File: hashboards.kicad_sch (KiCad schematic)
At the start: 5 parts, among them J10 Hashboard3, J4 Hashboard0, J5 Hashboard1, J9 Hashboard2, U10 PCA9546ARGVR

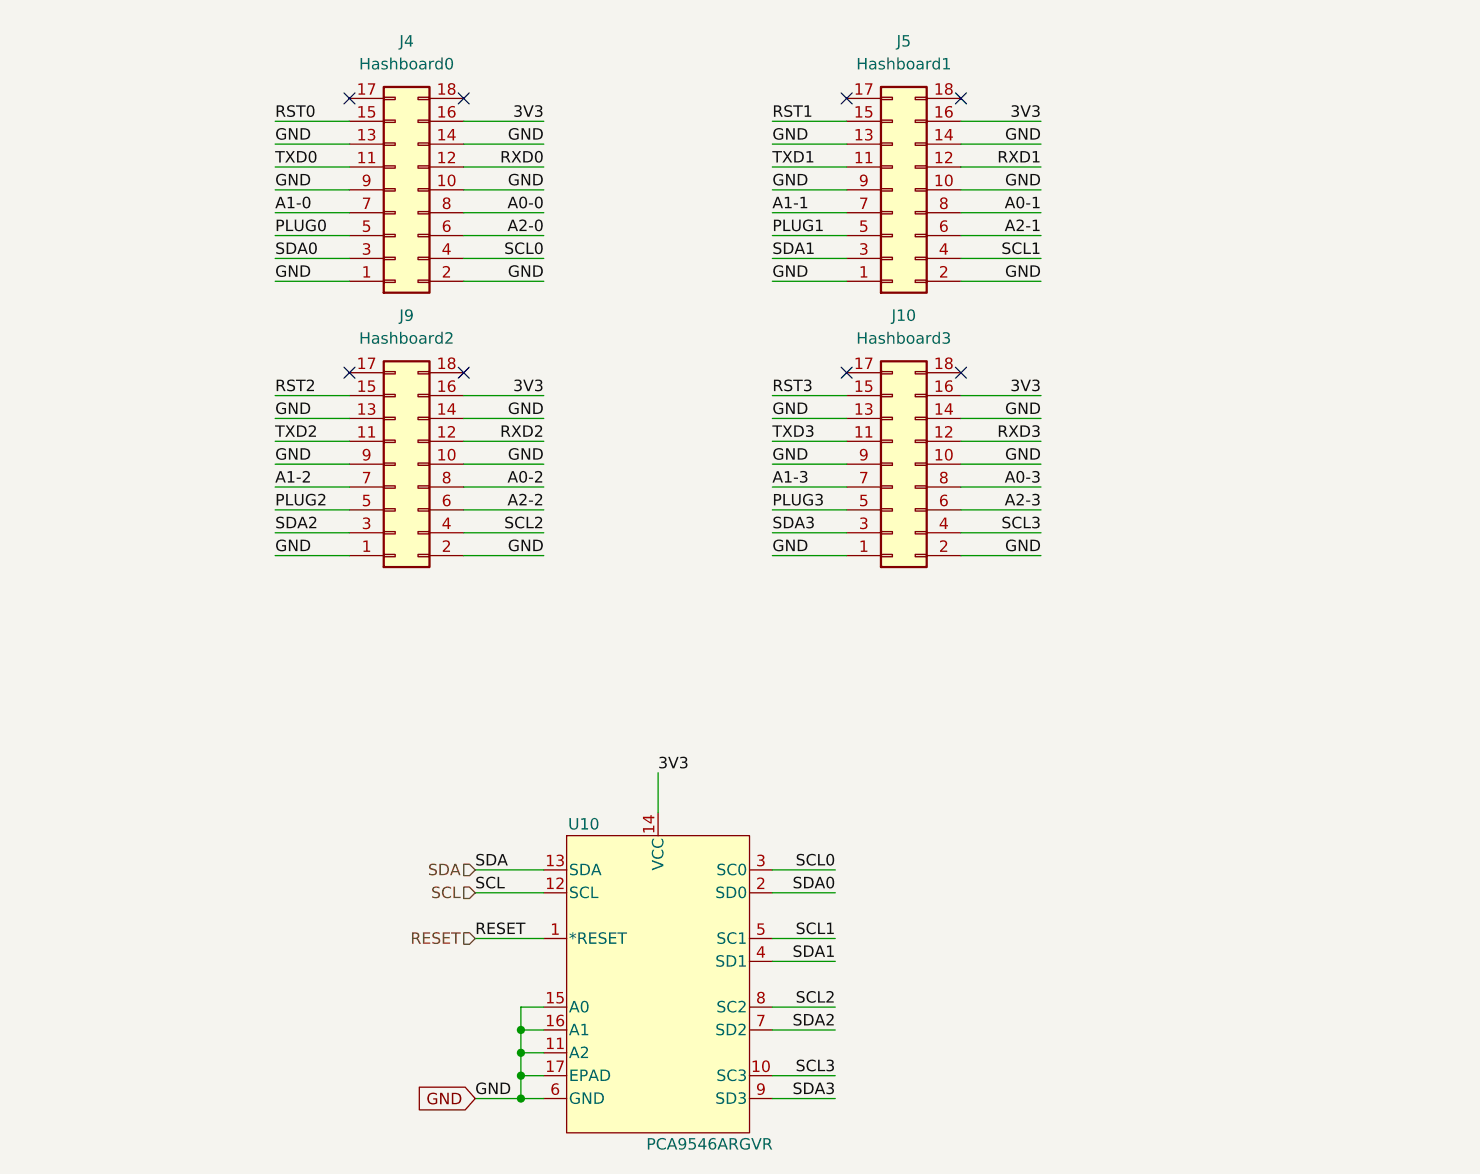
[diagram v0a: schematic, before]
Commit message: extended the board to make room for IO connectors. added the vertical display connector.
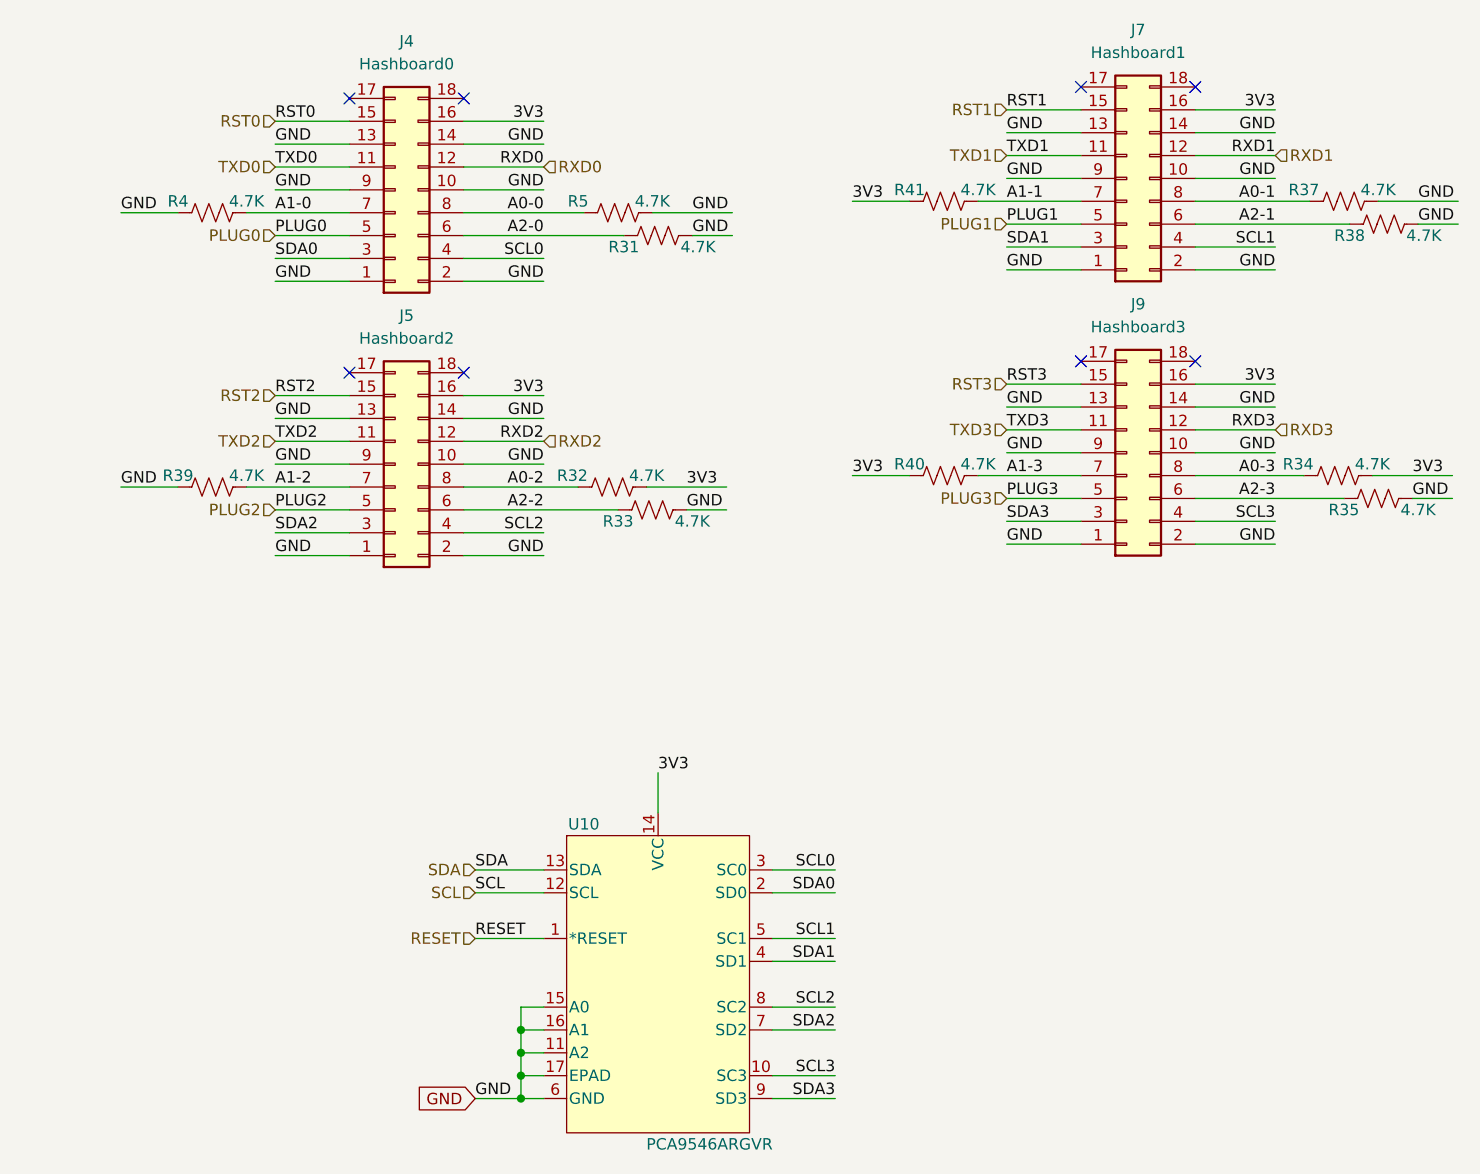
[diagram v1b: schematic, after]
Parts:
- removed J10: Hashboard3, bitcart:CONN-SMD_X2026WRS-2X09D-LPSW, symbol Connector_Generic:Conn_02x09_Odd_Even
- added J7: Hashboard1, bitcart:CONN-TH_X2026WV-2-09D-46SN, symbol Connector_Generic:Conn_02x09_Odd_Even
- added R31, R32, R33, R34, R35, R37, R38, R39, R4, R40, R41, R5: 4.7K, Resistor_SMD:R_0402_1005Metric, symbol Device:R_US
- J4: footprint bitcart:CONN-SMD_X2026WRS-2X09D-LPSW -> bitcart:CONN-TH_X2026WV-2-09D-46SN; LCSC C718164 -> C437089; PARTNO X2026WRS-2x09D-LPSW -> X2026WV-2x09D-46SN
- J5: value Hashboard1 -> Hashboard2; footprint bitcart:CONN-SMD_X2026WRS-2X09D-LPSW -> bitcart:CONN-TH_X2026WV-2-09D-46SN; LCSC C718164 -> C437089; PARTNO X2026WRS-2x09D-LPSW -> X2026WV-2x09D-46SN
- J9: value Hashboard2 -> Hashboard3; footprint bitcart:CONN-SMD_X2026WRS-2X09D-LPSW -> bitcart:CONN-TH_X2026WV-2-09D-46SN; LCSC C718164 -> C437089; PARTNO X2026WRS-2x09D-LPSW -> X2026WV-2x09D-46SN
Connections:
- net 3V3: now also J7.16 (Pin_16), R32.2, R34.2, R40.1, R41.1
- net A0-0: now also R5.1
- net A0-1: now also J7.8 (Pin_8), R37.1; no longer J5.8 (Pin_8)
- net A0-2: now also J5.8 (Pin_8), R32.1; no longer J9.8 (Pin_8)
- net A0-3: now also J9.8 (Pin_8), R34.1
- net A1-0: now also R4.2
- net A1-1: now also J7.7 (Pin_7), R41.2; no longer J5.7 (Pin_7)
- net A1-2: now also J5.7 (Pin_7), R39.2; no longer J9.7 (Pin_7)
- net A1-3: now also J9.7 (Pin_7), R40.2
- net A2-0: now also R31.1
- net A2-1: now also J7.6 (Pin_6), R38.1; no longer J5.6 (Pin_6)
- net A2-2: now also J5.6 (Pin_6), R33.1; no longer J9.6 (Pin_6)
- net A2-3: now also J9.6 (Pin_6), R35.1
- net GND: now also J7.1 (Pin_1), J7.10 (Pin_10), J7.13 (Pin_13), J7.14 (Pin_14), J7.2 (Pin_2), J7.9 (Pin_9), R31.2, R33.2, R35.2, R37.2, R38.2, R39.1, R4.1, R5.2
- net PLUG1: now also J7.5 (Pin_5); no longer J5.5 (Pin_5)
- net PLUG2: now also J5.5 (Pin_5); no longer J9.5 (Pin_5)
- net PLUG3: now also J9.5 (Pin_5)
- net RST1: now also J7.15 (Pin_15); no longer J5.15 (Pin_15)
- net RST2: now also J5.15 (Pin_15); no longer J9.15 (Pin_15)
- net RST3: now also J9.15 (Pin_15)
- net RXD1: now also J7.12 (Pin_12); no longer J5.12 (Pin_12)
- net RXD2: now also J5.12 (Pin_12); no longer J9.12 (Pin_12)
- net RXD3: now also J9.12 (Pin_12)
- net SCL1: now also J7.4 (Pin_4); no longer J5.4 (Pin_4)
- net SCL2: now also J5.4 (Pin_4); no longer J9.4 (Pin_4)
- net SCL3: now also J9.4 (Pin_4)
- net SDA1: now also J7.3 (Pin_3); no longer J5.3 (Pin_3)
- net SDA2: now also J5.3 (Pin_3); no longer J9.3 (Pin_3)
- net SDA3: now also J9.3 (Pin_3)
- net TXD1: now also J7.11 (Pin_11); no longer J5.11 (Pin_11)
- net TXD2: now also J5.11 (Pin_11); no longer J9.11 (Pin_11)
- net TXD3: now also J9.11 (Pin_11)

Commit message: resolved some schematic-board errors. switched to tap-on-top ethernet.
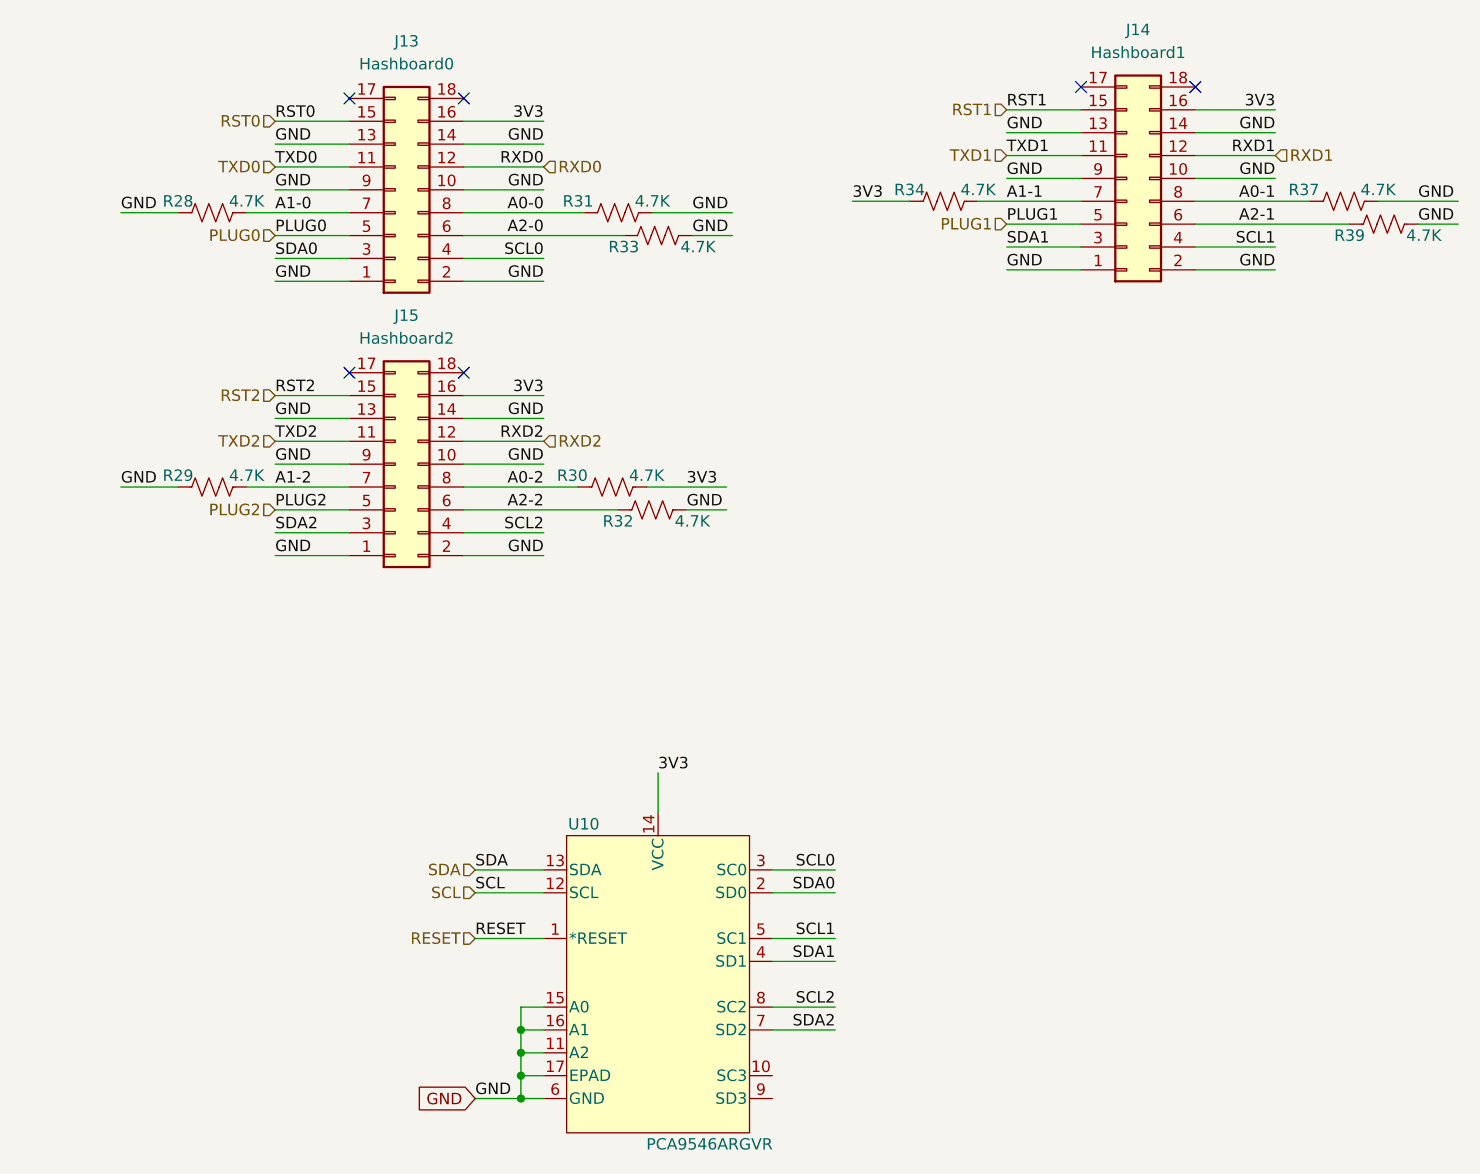
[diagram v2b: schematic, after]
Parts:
- removed J9: Hashboard3, bitcart:CONN-TH_X2026WV-2-09D-46SN, symbol Connector_Generic:Conn_02x09_Odd_Even
- removed R34, R35, R40: 4.7K, Resistor_SMD:R_0402_1005Metric, symbol Device:R_US
- renumbered J4 to J13, J7 to J14, J5 to J15, R4 to R28, R39 to R29, R32 to R30, R5 to R31, R33 to R32, R31 to R33, R41 to R34, R38 to R39
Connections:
- net SCL3: no longer names the net of U10.10 (SC3)
- net SDA3: no longer names the net of U10.9 (SD3)
- no-connect marks 8 -> 6

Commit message: pulled in bitcrane fan and data connectors and edge cuts. most placement done. started routing
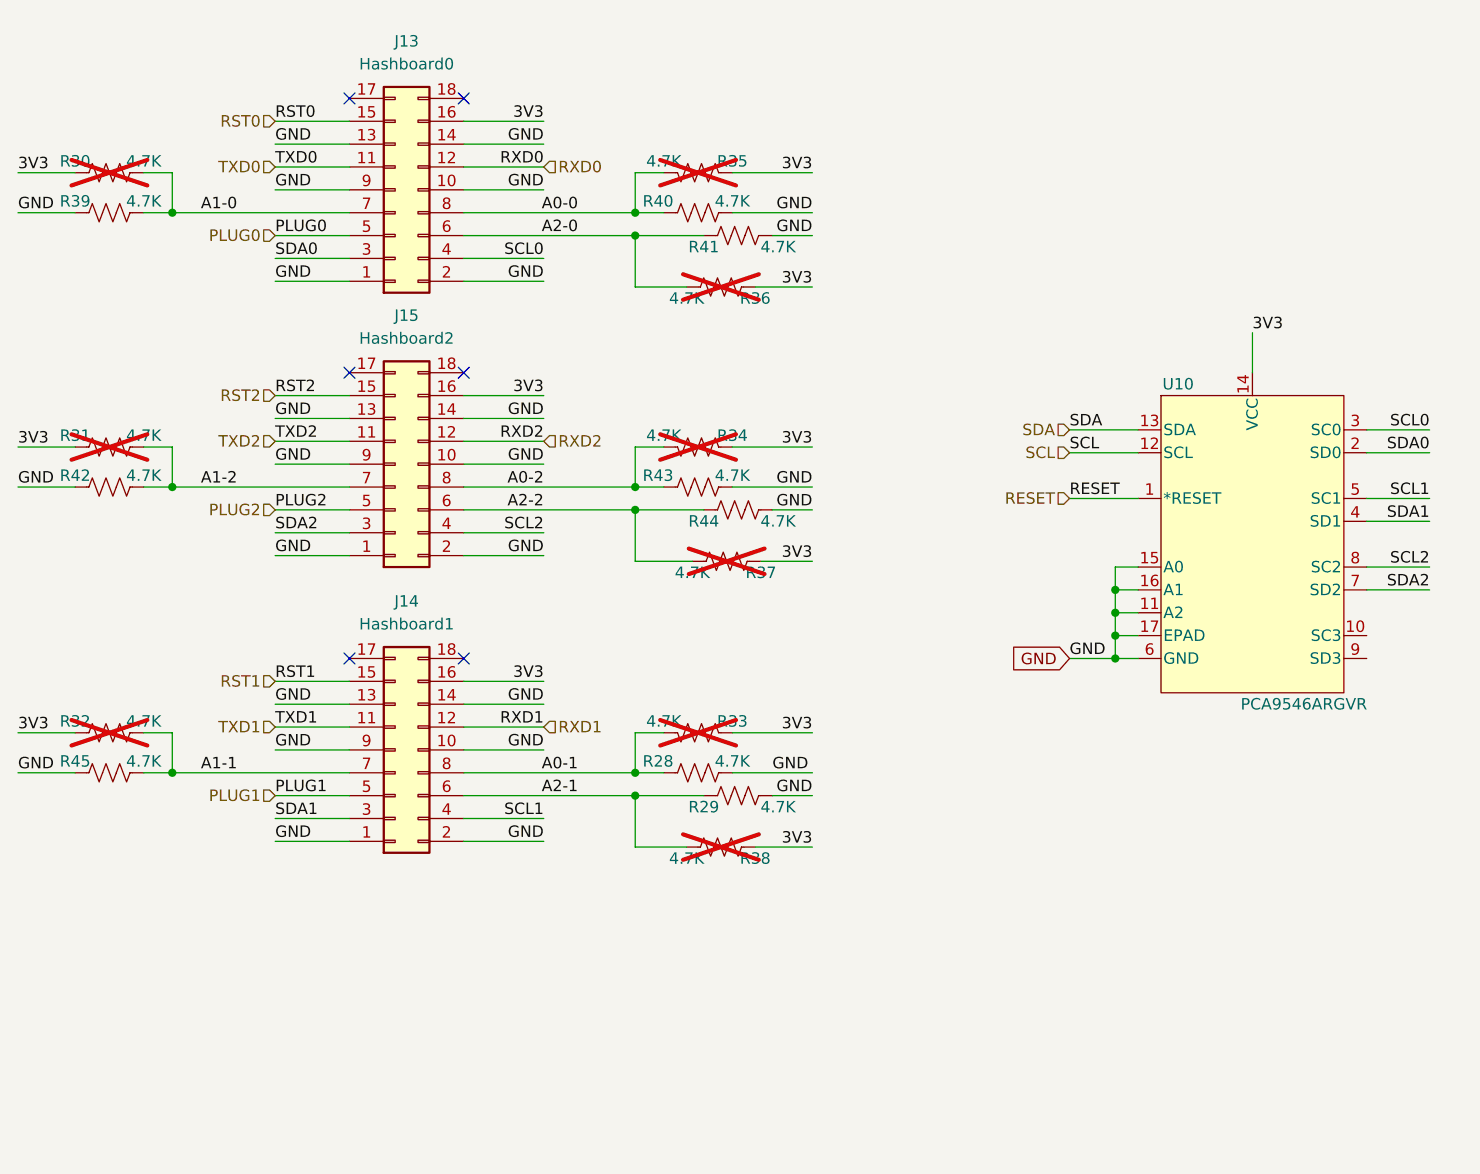
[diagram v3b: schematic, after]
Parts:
- added R35, R36, R38, R40, R41, R42, R43, R44, R45: 4.7K, Resistor_SMD:R_0805_2012Metric, symbol Device:R_US
- R28, R29, R39: footprint Resistor_SMD:R_0402_1005Metric -> Resistor_SMD:R_0805_2012Metric; DK (none) -> 311-4.70KCRCT-ND; PARTNO (none) -> RC0805FR-074K7L
- R30, R31, R32, R33, R34, R37: footprint Resistor_SMD:R_0402_1005Metric -> Resistor_SMD:R_0805_2012Metric; DK (none) -> 311-4.70KCRCT-ND; PARTNO (none) -> RC0805FR-074K7L; now not fitted
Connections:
- net 3V3: now also R30.1, R31.1, R32.1, R33.1, R37.1, R35.1, R36.1, R38.1; no longer R30.2
- net A0-0: now also R35.2, R40.1; no longer R31.1
- net A0-1: now also R28.1, R33.2; no longer R37.1
- net A0-2: now also R34.2, R43.1; no longer R30.1
- net A1-0: now also R30.2, R39.2; no longer R28.2
- net A1-1: now also R32.2, R45.2; no longer R34.2
- net A1-2: now also R31.2, R42.2; no longer R29.2
- net A2-0: now also R36.2, R41.1; no longer R33.1
- net A2-1: now also R29.1, R38.2; no longer R39.1
- net A2-2: now also R37.2, R44.1; no longer R32.1
- net GND: now also R28.2, R29.2, R39.1, R40.2, R41.2, R42.1, R43.2, R44.2, R45.1; no longer R28.1, R29.1, R31.2, R32.2, R33.2, R37.2, R39.2
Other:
- moved on the sheet: J14, U10

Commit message: lots of routing. lots more to do
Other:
- moved on the sheet: J14, J15, R28, R29, R31, R32, R33, R34, R37, R38, R42, R43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
